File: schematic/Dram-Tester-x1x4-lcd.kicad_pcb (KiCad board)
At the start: 2 copper layers, 100 x 100 mm, 56 parts, among them IC1 TC7660S, J1 MJ-179PH, J2 PS, SW1 DTS-63N-V, SW2 SS12SDP2, SW3 SS22SDP2, U1 Arduino Nano, U2 MT3608 DCDC Module, U3 I2C OLED Screen 0.91in. 128x32, U4 (AL12832AWWB-H-U02)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

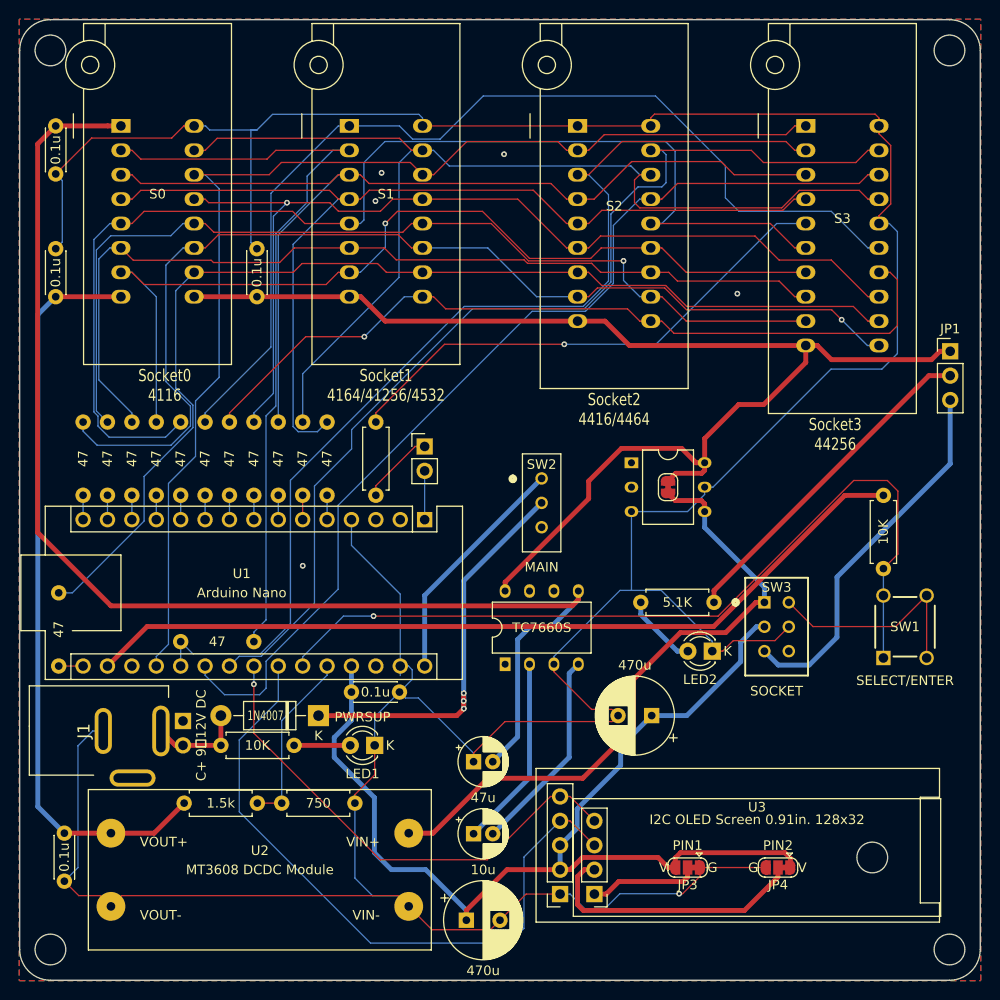
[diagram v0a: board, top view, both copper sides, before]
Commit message: Schematic modified
回路図を修正
Schematic modified.
積層セラミックコンデンサのピッチを2.5mmに変更
Changed pitch of MLCC to 2.5 mm.
未実装の5V-DCDCモジュールを削除
Remove unmounted 5V-DCDC module
重複していたパスコンを削除
Removed duplicated bypass capacitor.
47μFの電解コンデンサを10μFに変更
47uF ELC changed to 10uF.
チャージポンプの品番をTC7660SからTJ7660に変更
The part number of the charge pump was changed from TC7660S to TJ7660.
その他細かな修正
Other minor modifications.
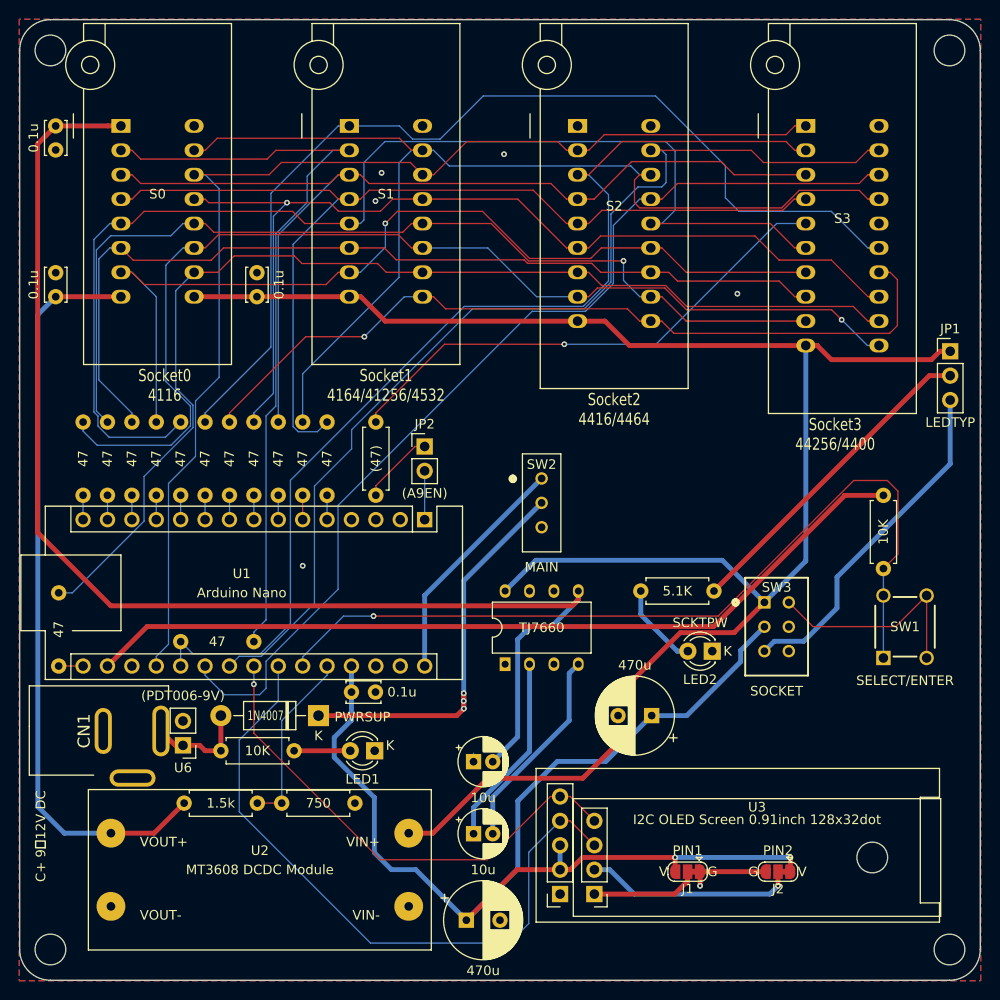
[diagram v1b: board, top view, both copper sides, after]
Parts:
- removed C9: 470u, Capacitor_THT:CP_Radial_D8.0mm_P3.50mm
- removed JP3: PIN1, Jumper:SolderJumper-3_P1.3mm_Bridged12_RoundedPad1.0x1.5mm
- removed JP4: PIN2, Jumper:SolderJumper-3_P1.3mm_Bridged12_RoundedPad1.0x1.5mm
- removed JP5: A9EN, Connector_PinHeader_2.54mm:PinHeader_1x02_P2.54mm_Vertical
- removed U5: (AE-XCL103-5V0), ProjectLibrary:DIP6_300mil_FineLongPad_No3D
- added CN1: MJ-179PH, ProjectLibrary:MJ179PH, F.Cu at (109.6, 118.4)
- added U6: (PDT006-9V), Connector_PinHeader_2.54mm:PinHeader_1x02_P2.54mm_Vertical, F.Cu at (117.9, 119.9)
- C1, C2, C3, C4: footprint Capacitor_THT:C_Disc_D4.3mm_W1.9mm_P5.00mm -> Capacitor_THT:C_Disc_D3.4mm_W2.1mm_P2.50mm
- C6: value 47u -> 10u
- C8: value 0.1u -> 470u; footprint Capacitor_THT:C_Disc_D4.3mm_W1.9mm_P5.00mm -> Capacitor_THT:CP_Radial_D8.0mm_P3.50mm
- IC1: value TC7660S -> TJ7660
- J1: value MJ-179PH -> PIN1; footprint ProjectLibrary:MJ179PH -> Jumper:SolderJumper-3_P1.3mm_Bridged12_RoundedPad1.0x1.5mm
- J2: value PS -> PIN2; footprint ProjectLibrary:PinHeader_1x02_P2.54mm_Vertical_noSilk -> Jumper:SolderJumper-3_P1.3mm_Bridged12_RoundedPad1.0x1.5mm
- JP1: value Pin Header 1x3pin -> LEDTYP
- JP2: value 5V -> (A9EN); footprint Jumper:SolderJumper-2_P1.3mm_Bridged_RoundedPad1.0x1.5mm -> Connector_PinHeader_2.54mm:PinHeader_1x02_P2.54mm_Vertical
- LED2: value Green -> SCKTPW
- R19: value 47 -> (47)
- U3: value I2C OLED Screen 0.91in. 128x32 -> I2C OLED Screen 0.91inch 128x32dot
- moved J2 63.9 mm to (179.9, 133.1), turned to 180 degrees
- moved J1 62.6 mm to (170.5, 133.1)
- moved C8 62.4 mm to (166.7, 116.8), turned to 180 degrees
- moved JP2 25.7 mm to (143.1, 88.8), turned to 0 degrees
- moved C1 5.00 mm to (104.7, 55.4), turned to -90 degrees
- moved C2 2.50 mm to (104.7, 70.7)
- moved C4 2.50 mm to (138.0, 114.4), turned to 180 degrees
- moved R18 1.18 mm to (165.6, 103.9)
- moved LED1 0.56 mm to (137.9, 120.5)
- moved R17 0.56 mm to (129.5, 120.5)
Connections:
- C1 pad 1: GND -> -5V
- C1 pad 2: -5V -> GND
- C4 pad 1: +5V -> GND
- C4 pad 2: GND -> +5V
- C8 pad 1: +12V -> +5V
- J1 pad 2: unconnected-(J1-B-Pad2) -> Net-(J1-C)
- J1 pad 3: /NPPS -> +5V
- J2 pad 1: GND -> +5V
- J2 pad 2: /NPPS -> Net-(J2-C)
- JP2 pad 1: SOCKET_PS -> Net-(JP2-A)
- JP2 pad 2: SOCKET_5V -> Net-(JP2-B)
- R19 pad 2: Net-(JP5-A) -> Net-(JP2-A)
- SW3 pad 1: SOCKET_PS -> SOCKET_5V
- U1 pad 1: Net-(JP5-B) -> Net-(JP2-B)
- U2 pad 1: SOCKET_PS -> SOCKET_5V
- U3 pad 1: Net-(JP3-C) -> Net-(J1-C)
- U3 pad 2: Net-(JP4-C) -> Net-(J2-C)
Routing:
- net GND: track 402.3 -> 9.48 mm
- net SOCKET_PS: track 67.0 -> 0.00 mm
- net SOCKET_5V: track 134.1 -> 190.4 mm
- net Net-(JP4-C): track 28.5 -> 0.00 mm
- net Net-(J2-C): track 0.00 -> 22.0 mm, vias 0 -> 1
- net +5V: track 111.6 -> 124.8 mm, vias 0 -> 2
- net Net-(JP3-C): track 11.4 -> 0.00 mm
- net Net-(J1-C): track 0.00 -> 11.2 mm
- net Net-(JP5-A): track 7.79 -> 0.00 mm
- net Net-(JP2-A): track 0.00 -> 7.79 mm
- net Net-(JP5-B): track 5.08 -> 0.00 mm
- net Net-(JP2-B): track 0.00 -> 5.08 mm
- net SOCKET_OFF: track 38.9 -> 36.0 mm
- net Net-(JP1-C): track 35.1 -> 33.9 mm
- net Net-(LED2-A): track 7.75 -> 8.93 mm
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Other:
- board text added: "1bit and 4bit support standalone DRAM tester with display rev.3 by Goripon Hardware. 4116/4164/41256/4532/4416/4464/44256/4400 supported."
- board text added: "Socket3 44256/4400"
- board text removed: "1&4 bit support standalone DRAM tester with display by Goripon Hardware. 4116/4164/41256/4532/4416/4464/44256 supported."
- board text removed: "Socket3 44256"

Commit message: Modified Schematic & README
Modified Schematic & README
回路図および基板のリビジョンを4に更新し部品番号のシルク印刷の欠落を修正
Updated schematic and PCB revision to 4 and fixed missing part number silkscreen.
READMEの準備項に頒布品に関する記載を追加
Added information about distribution items to the preparation section of the README.
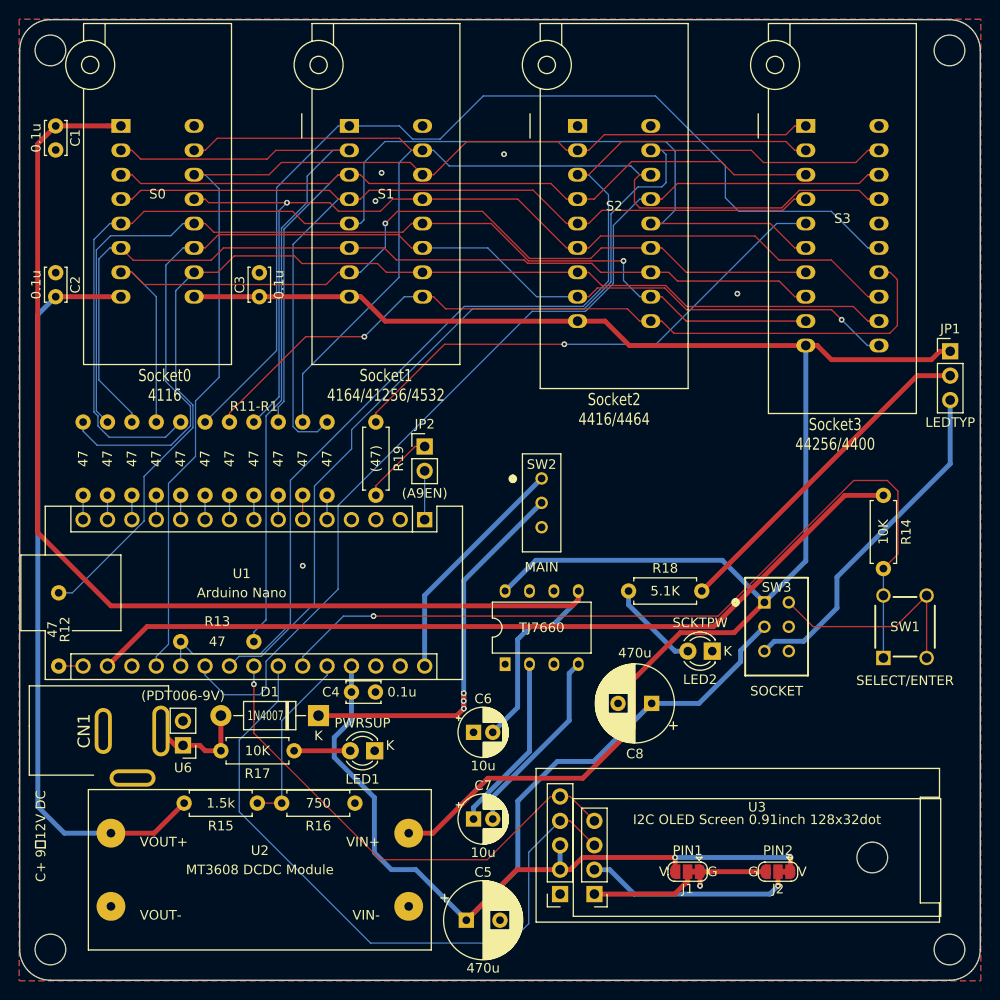
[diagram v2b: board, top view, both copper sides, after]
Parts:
- moved C6 3.06 mm to (148.2, 118.6)
- moved C7 1.53 mm to (148.2, 127.6)
- moved R18 1.27 mm to (164.3, 103.9)
- moved C8 1.27 mm to (166.7, 115.6)
- moved C3 0.25 mm to (125.9, 73.2)
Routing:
- net -5V: track 133.3 -> 130.2 mm
- net Net-(IC1-CAP-): track 21.3 -> 19.8 mm
- net Net-(IC1-CAP+): track 20.1 -> 18.5 mm
- net Net-(JP1-C): track 33.9 -> 35.2 mm
- net GND: track 9.48 -> 8.59 mm
- net Net-(LED2-A): track 8.93 -> 9.61 mm
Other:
- board text added: "R11-R1"
